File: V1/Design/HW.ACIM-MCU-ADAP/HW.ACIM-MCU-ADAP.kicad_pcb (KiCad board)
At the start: 4 copper layers, 81.1 x 67.8 mm, 138 parts, among them J1 U, J101 HEADER 2x15POS, J102 HEADER 2x15POS, J2 V, J3 W, J4 PGND, J5 QWIIC, U1 ISO OPAMP 1-CH, U101 MIPS 32-bit DSC, U102 24MHz, U15 ISO OPAMP 1-CH, U17 OP-1CH, U2 ISO OPAMP 1-CH, U3 OP-1CH, U4 OP-1CH, U5 LDO 3.3V

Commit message: HW.ACIM-MCU-ADAP schematic update 5
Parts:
- TP1: value AVDD -> UU
- TP2: value AVDD -> UV
- TP3: value AVDD -> UW
- TP4: value GND ISO -> GND*
- TP5: value 3V3 ISO -> 3V3*
- TP6: value UU DIV -> UU*
- TP7: value UV DIV -> UV*
- TP8: value UW DIV -> UW*
- moved TP102 51.7 mm to (227.2, 89.9)
- moved TP1 49.8 mm to (204.5, 91.3)
- moved TP101 48.9 mm to (222.9, 88.7)
- moved C23 48.1 mm to (212.7, 106.9), turned to -90 degrees
- moved FT8 40.0 mm to (211.5, 106.9), turned to -90 degrees
- moved C21 37.1 mm to (203.0, 95.5), turned to 135 degrees
- moved TP103 37.0 mm to (202.2, 101.9)
- moved C101 35.9 mm to (207.5, 91.0), turned to -45 degrees
- moved C22 35.9 mm to (202.2, 96.3), turned to 135 degrees
- moved C25 34.7 mm to (204.7, 93.8), turned to 135 degrees
- moved C26 33.5 mm to (203.9, 94.6), turned to 135 degrees
- moved C27 31.0 mm to (201.3, 97.2), turned to 135 degrees
- moved TP104 30.8 mm to (199.9, 99.4)
- moved FT6 28.1 mm to (201.6, 94.0), turned to -45 degrees
- moved FT7 26.9 mm to (200.7, 94.9), turned to -45 degrees
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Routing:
- net +3V3_MCU: track 118.9 -> 175.8 mm, vias 2 -> 7
- net AGND_MCU: track 37.4 -> 94.2 mm, vias 5 -> 11
- net /MCU/MC_UU: track 1.20 -> 38.1 mm, vias 0 -> 2
- net /MCU/MC_UV: track 1.20 -> 33.1 mm, vias 0 -> 2
- net /MCU/~{MCLR}: track 0.00 -> 31.6 mm
- net /MCU/MC_UW: track 1.20 -> 29.5 mm, vias 0 -> 2
- net /MCU/MC_IU: track 0.00 -> 23.7 mm, vias 1 -> 2
- net /MCU/PWR_RELAY: track 0.00 -> 20.3 mm, vias 1 -> 2
- net /MCU/UDC_DIV: track 0.00 -> 10.3 mm
- net /MCU/MC_UW_DIV: track 0.00 -> 8.98 mm
- net /MCU/SLED: track 9.95 -> 17.5 mm
- net /MCU/IDC_SEN: track 0.00 -> 5.76 mm
- net /MCU/MC_UV_DIV: track 0.00 -> 5.02 mm
- net /MCU/MC_UU_DIV: track 0.00 -> 4.73 mm
- net /MCU/MC_IU_SEN: track 1.20 -> 4.97 mm, vias 1 -> 0
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
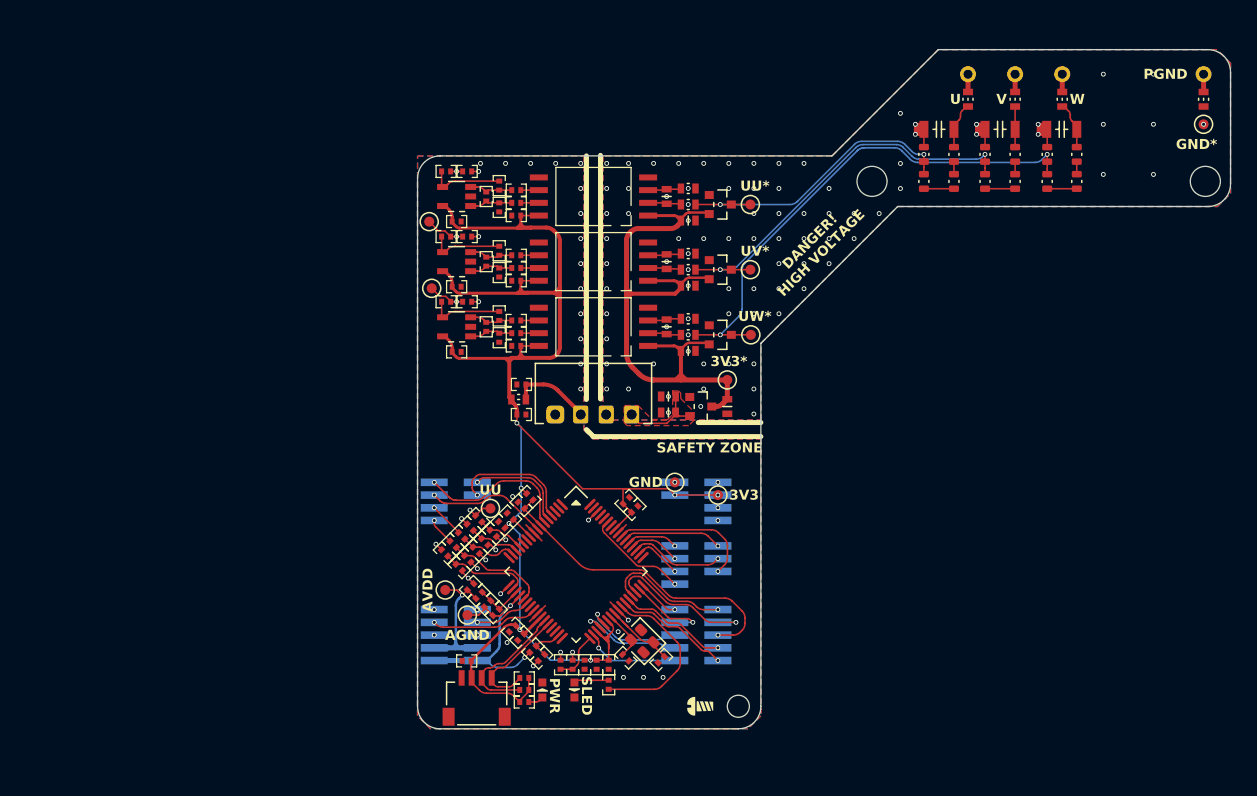
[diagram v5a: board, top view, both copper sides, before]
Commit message: HW.ACIM-MCU-ADAP layout & production
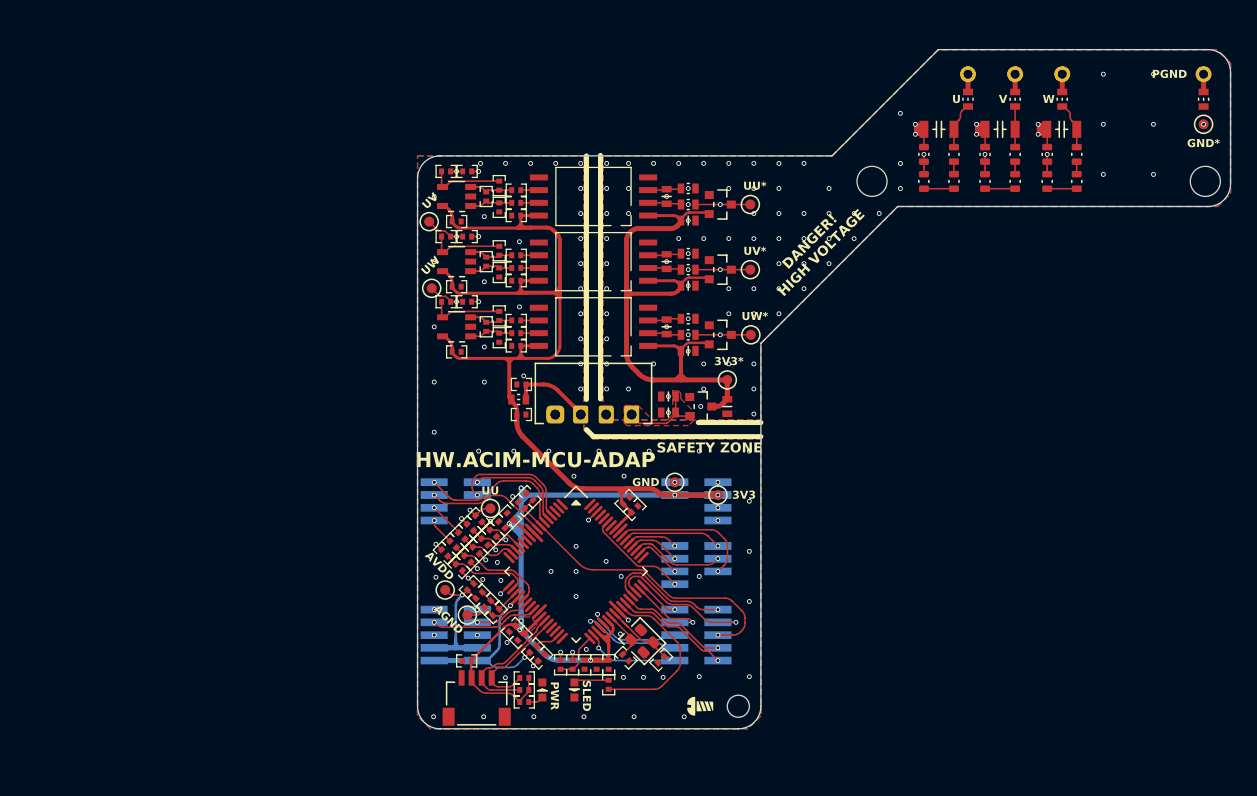
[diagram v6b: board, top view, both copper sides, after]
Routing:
- net AGND_MCU: track 94.2 -> 46.1 mm
- net +3V3_MCU: track 175.8 -> 198.6 mm
- net GND_ISO: track 20.1 -> 23.1 mm
- net GND_MCU: track 8.20 -> 7.07 mm, vias 25 -> 71
- added copper zone on F.Cu, net +3V3_MCU
- added copper zone on In1.Cu, net AGND_MCU
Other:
- board text added: "HW.ACIM-MCU-ADAP"
